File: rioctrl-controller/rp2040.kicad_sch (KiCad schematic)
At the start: 44 parts, among them J2 PIN_HEADER_3V, J3 TYPE-C-31-M-12, J4 Conn_02x05_Odd_Even, J5 PIN_HEADER_3V, SW1 SW_PUSH_SMALL, U5 W25Q16JVSS, U6 USBLC6-4SC6, U7 RP2040, Y1 Crystal_12MHz

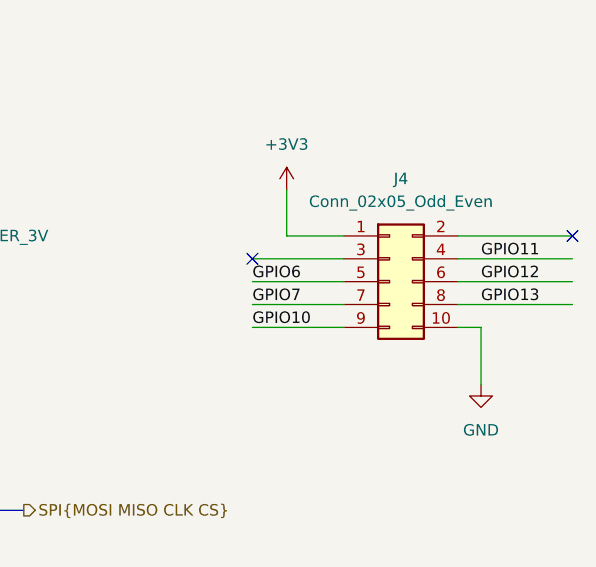
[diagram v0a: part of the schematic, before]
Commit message: Ditch the separate backplane board, increase the slot bitwidth to 12
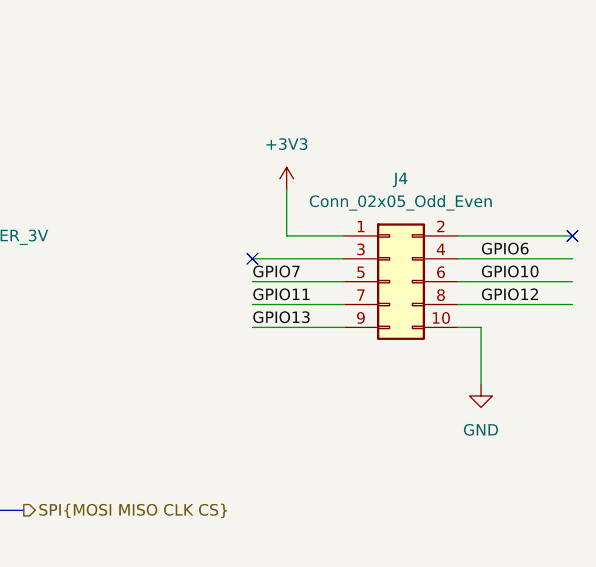
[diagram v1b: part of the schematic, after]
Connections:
- net GPIO10: now also J4.6 (Pin_6); no longer J4.9 (Pin_9)
- net GPIO11: now also J4.7 (Pin_7); no longer J4.4 (Pin_4)
- net GPIO12: now also J4.8 (Pin_8); no longer J4.6 (Pin_6)
- net GPIO13: now also J4.9 (Pin_9); no longer J4.8 (Pin_8)
- net GPIO6: now also J4.4 (Pin_4); no longer J4.5 (Pin_5)
- net GPIO7: now also J4.5 (Pin_5); no longer J4.7 (Pin_7)
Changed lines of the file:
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@@
 	(label "SPI.CLK"
 		(at 241.3 93.98 0)
+		(fields_autoplaced yes)
 		(effects
 			(font
@@
 	)
 	(label "GPIO6"
-		(at 330.2 93.98 0)
+		(at 355.6 91.44 0)
 		(fields_autoplaced yes)
 		(effects
@@
 	(label "SPI.MISO"
 		(at 241.3 99.06 0)
+		(fields_autoplaced yes)
 		(effects
 			(font
@@
 	)
 	(label "GPIO13"
-		(at 355.6 96.52 0)
+		(at 330.2 99.06 0)
 		(fields_autoplaced yes)
 		(effects
@@
 	)
 	(label "GPIO12"
-		(at 355.6 93.98 0)
+		(at 355.6 96.52 0)
 		(fields_autoplaced yes)
 		(effects
@@
 	(label "SPI.CS"
 		(at 241.3 101.6 0)
+		(fields_autoplaced yes)
 		(effects
 			(font
@@
 	)
 	(label "GPIO7"
-		(at 330.2 96.52 0)
+		(at 330.2 93.98 0)
 		(fields_autoplaced yes)
 		(effects
@@
 	)
 	(label "GPIO11"
-		(at 355.6 91.44 0)
+		(at 330.2 96.52 0)
 		(fields_autoplaced yes)
 		(effects
@@
 	)
 	(label "GPIO10"
-		(at 330.2 99.06 0)
+		(at 355.6 93.98 0)
 		(fields_autoplaced yes)
 		(effects
@@
 	(label "SPI.MOSI"
 		(at 241.3 96.52 0)
-		(effects
-			(font
+		(fields_autoplaced yes)
+		(effects
+			(font

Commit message: Fix ERC, add title information to sch, add initial version of build scripts
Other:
- company: (none) -> R. Veips
- title: (none) -> ${PROJECTNAME}
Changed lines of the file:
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@@
 	(generator_version "8.0")
 	(paper "A3")
+	(title_block
+		(title "${PROJECTNAME}")
+		(date "2024-08-25")
+		(rev "${VERSION}")
+		(company "R. Veips")
+	)
 	(junction
 		(at 115.57 68.58)

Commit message: Fill in BOM (LCSC#)
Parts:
- J4, JP1, TP7, TP8, TP9: now not fitted
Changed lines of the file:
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@@
 		(in_bom yes)
 		(on_board yes)
-		(dnp no)
+		(dnp yes)
 		(fields_autoplaced yes)
 		(property "Reference" "J4"
@@
 		(in_bom no)
 		(on_board yes)
-		(dnp no)
+		(dnp yes)
 		(fields_autoplaced yes)
 		(property "Reference" "JP1"
@@
 		(in_bom no)
 		(on_board yes)
-		(dnp no)
+		(dnp yes)
 		(fields_autoplaced yes)
 		(property "Reference" "TP9"
@@
 		(in_bom no)
 		(on_board yes)
-		(dnp no)
+		(dnp yes)
 		(fields_autoplaced yes)
 		(property "Reference" "TP7"
@@
 		(in_bom no)
 		(on_board yes)
-		(dnp no)
+		(dnp yes)
 		(fields_autoplaced yes)
 		(property "Reference" "TP8"

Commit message: Fix minor issues in rioctrl-controller, release v1.1
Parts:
- D9: now not fitted
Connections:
- net GND: now also Y1.2, Y1.4; no longer Y1.1, Y1.3
- net at C22.2, U7.20 (XIN): now also Y1.3; no longer Y1.2
- net at C23.2, U7.21 (XOUT): now also Y1.1; no longer Y1.4
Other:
- note added: "It's useless to power 5V rail here"
- moved on the sheet: Y1
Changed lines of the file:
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@@
 		)
 	)
+	(text "It's useless to power 5V rail here"
+		(exclude_from_sim no)
+		(at 180.34 203.2 0)
+		(effects
+			(font
+				(size 1.27 1.27)
+			)
+		)
+	)
 	(label "LED_RED"
 		(at 234.95 152.4 0)
@@
 	(symbol
 		(lib_id "hadv-mcu:Crystal_12MHz")
-		(at 121.92 127 0)
+		(at 121.92 127 90)
 		(unit 1)
 		(exclude_from_sim no)
@@
 		(dnp no)
 		(property "Reference" "Y1"
-			(at 132.08 123.4186 0)
+			(at 118.3386 116.84 0)
 			(effects
 				(font
@@
 		)
 		(property "Value" "Crystal_12MHz"
-			(at 134.62 125.73 0)
+			(at 120.65 114.3 0)
 			(effects
 				(font
@@
 		)
 		(property "Footprint" "Crystal:Crystal_SMD_2520-4Pin_2.5x2.0mm"
-			(at 119.38 135.89 0)
+			(at 130.81 129.54 0)
 			(effects
 				(font
@@
 		)
 		(property "MPN" "TXM12M0004252DBCEO00T"
-			(at 119.38 135.89 0)
+			(at 130.81 129.54 0)
 			(effects
 				(font
@@
 		)
 		(property "Manufacturer" "TAE(Zhejiang Abel Elec)"
-			(at 119.38 135.89 0)
+			(at 130.81 129.54 0)
 			(effects
 				(font
@@
 		)
 		(property "LCSC#" "C284154"
-			(at 121.285 135.89 0)
+			(at 130.81 127.635 0)
 			(effects
 				(font
@@
 		(in_bom yes)
 		(on_board yes)
-		(dnp no)
+		(dnp yes)
 		(fields_autoplaced yes)
 		(property "Reference" "D9"

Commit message: fix LCSC part number and MPN for R11 and R26
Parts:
- R26: LCSC# C112314 -> C14675; MPN RC0603FR-075K11L -> RC0603FR-07100KL
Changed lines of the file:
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@@
 			)
 		)
-		(property "LCSC#" "C112314"
+		(property "LCSC#" "C14675"
 			(at 285.75 161.29 0)
 			(effects
@@
 			)
 		)
-		(property "MPN" "RC0603FR-075K11L"
+		(property "MPN" "RC0603FR-07100KL"
 			(at 285.75 161.29 0)
 			(effects
